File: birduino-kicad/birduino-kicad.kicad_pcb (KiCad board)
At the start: 2 copper layers, 40.1 x 63.2 mm, 1 part, among them U1 ATMEGA328-PU

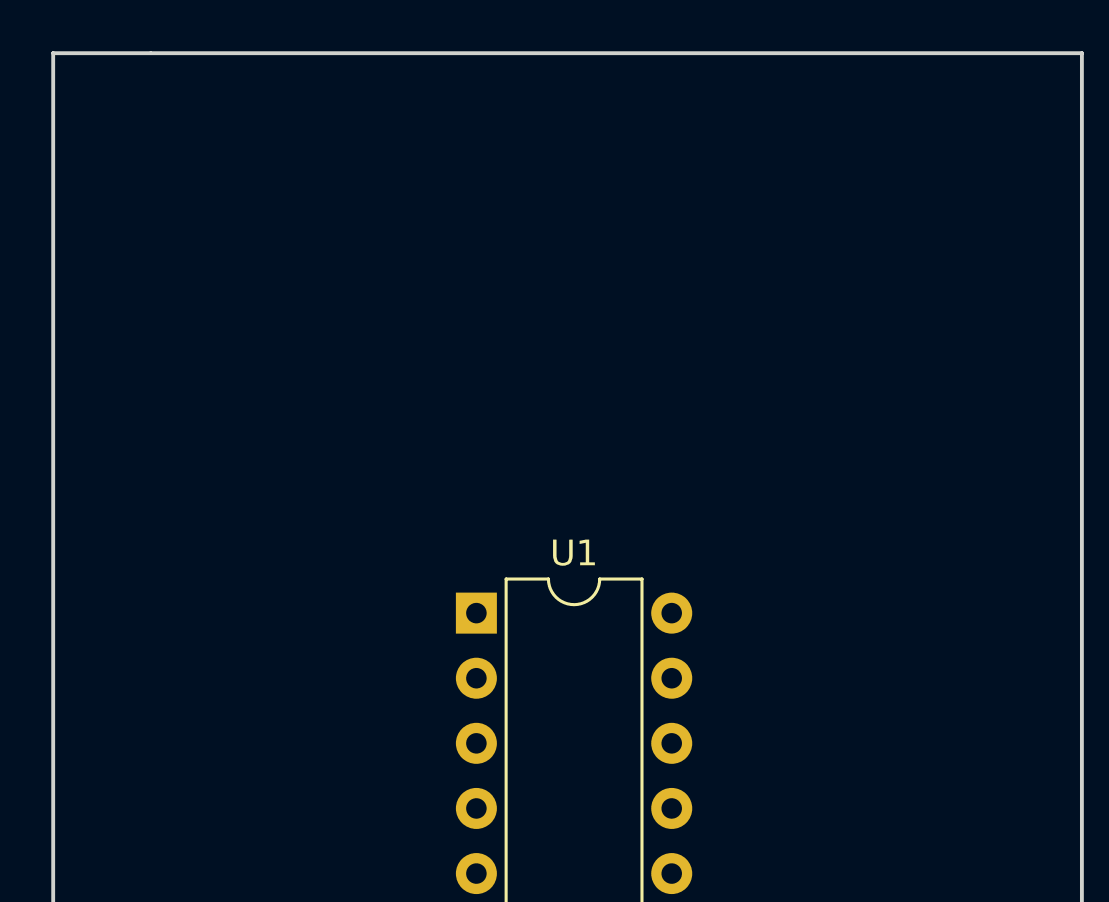
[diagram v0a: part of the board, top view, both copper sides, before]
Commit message: feat: Added more components to the board
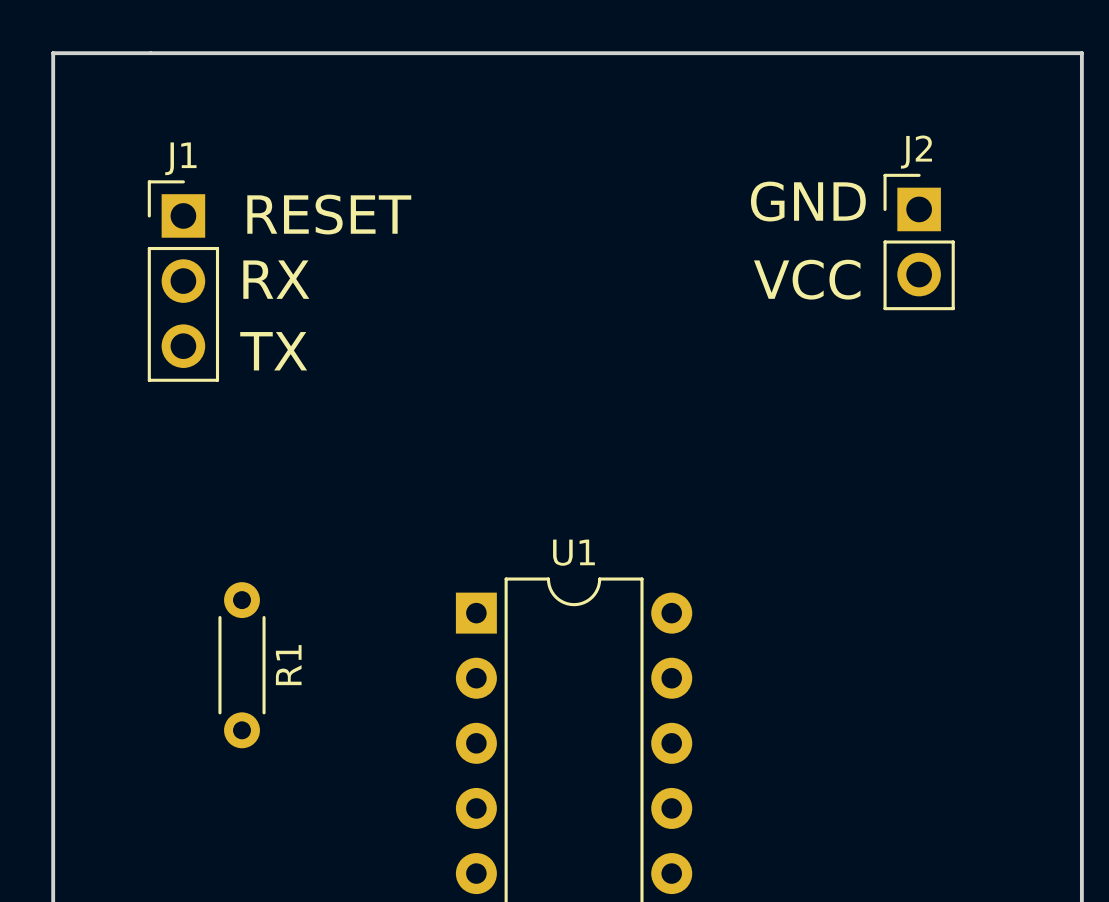
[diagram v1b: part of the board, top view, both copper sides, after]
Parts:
- added J1: Conn_01x03_Male, Pin_Headers:Pin_Header_Straight_1x03_Pitch2.54mm, F.Cu at (144.8, 65.5)
- added J2: Conn_01x02_Male, Pin_Headers:Pin_Header_Straight_1x02_Pitch2.54mm, F.Cu at (173.5, 65.3)
- added R1: 10k, Resistors_THT:R_Axial_DIN0204_L3.6mm_D1.6mm_P5.08mm_Horizontal, F.Cu at (147.1, 80.5)
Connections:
- U1 pad 1: (no net) -> Net-(J1-Pad1)
- U1 pad 2: (no net) -> Net-(J1-Pad2)
- U1 pad 20: (no net) -> Net-(J2-Pad2)
- U1 pad 22: (no net) -> GND
- U1 pad 3: (no net) -> Net-(J1-Pad3)
- U1 pad 7: (no net) -> Net-(J2-Pad2)
- U1 pad 8: (no net) -> GND
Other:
- board text added: "GND"
- board text added: "RESET"
- board text added: "RX"
- board text added: "TX"
- board text added: "VCC"

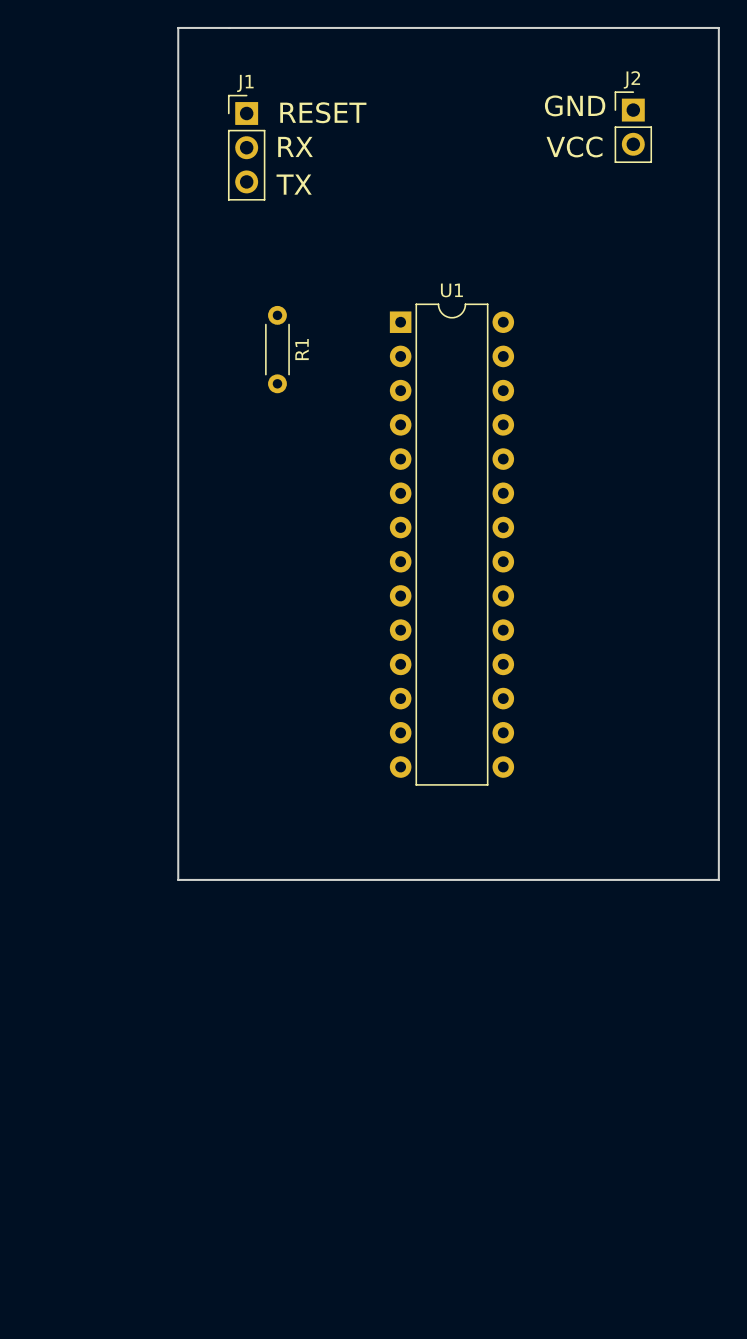
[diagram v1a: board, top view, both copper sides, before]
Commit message: feat: add radio card connections, added the first routing of vias, added backside label.
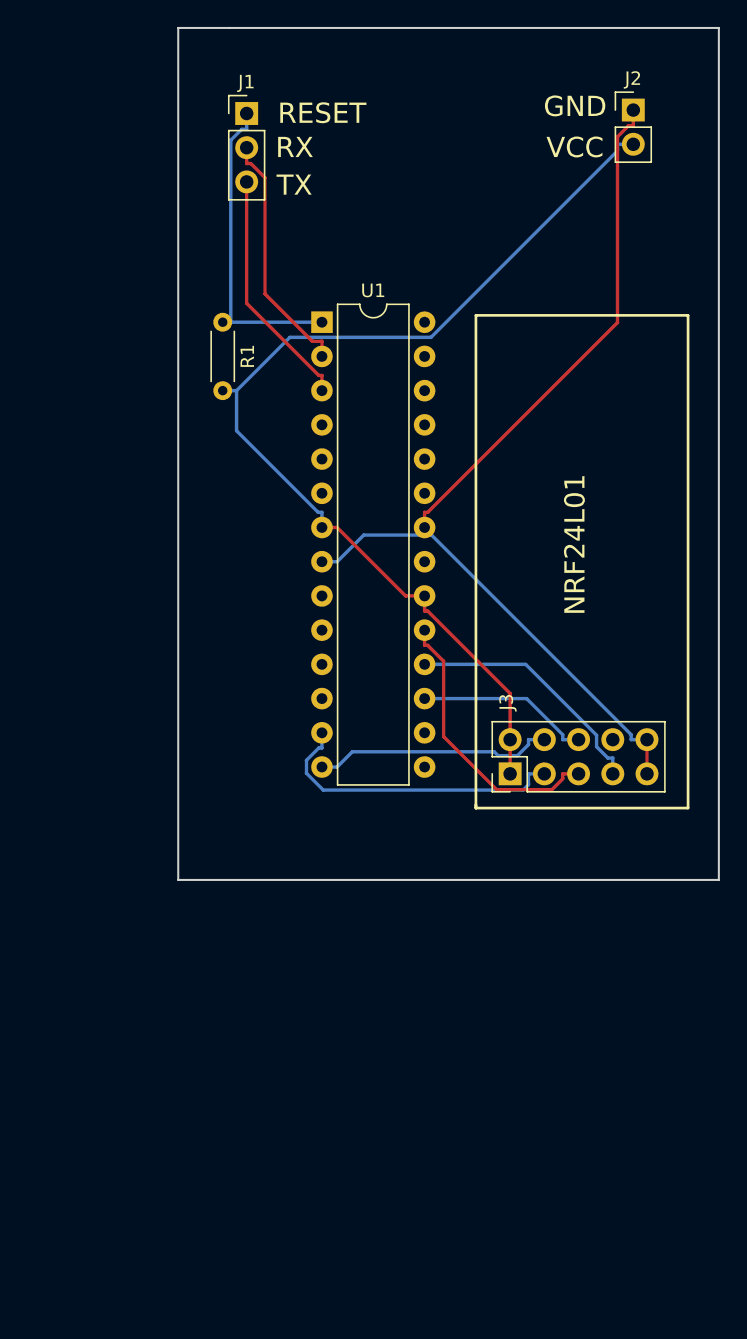
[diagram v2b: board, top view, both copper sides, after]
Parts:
- added J3: Conn_02x05_Odd_Even, Pin_Headers:Pin_Header_Straight_2x05_Pitch2.54mm, F.Cu at (164.3, 114.6)
- moved U1 5.84 mm to (150.4, 81.0)
- moved R1 4.10 mm to (143.0, 81.0)
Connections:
- net Net-(J2-Pad2) renamed VCC
- U1 pad 13: (no net) -> CE
- U1 pad 14: (no net) -> CSN
- U1 pad 17: (no net) -> MO
- U1 pad 18: (no net) -> MI
- U1 pad 19: (no net) -> SCK
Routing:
- net VCC: track 0.00 -> 77.0 mm
- net GND: track 0.00 -> 72.3 mm
- net Net-(J1-Pad1): track 0.00 -> 23.6 mm
- net CE: track 0.00 -> 22.8 mm
- net SCK: track 0.00 -> 21.0 mm
- net MI: track 0.00 -> 18.5 mm
- net Net-(J1-Pad2): track 0.00 -> 18.4 mm
- net Net-(J1-Pad3): track 0.00 -> 17.9 mm
- net CSN: track 0.00 -> 17.8 mm
- net MO: track 0.00 -> 12.9 mm
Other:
- board text added: "NRF24L01"
- board text added: "birduino v. 1.0 Designed in Berlin (02.2019)"

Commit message: feat: add footprint to the buttons, new routing with butons.
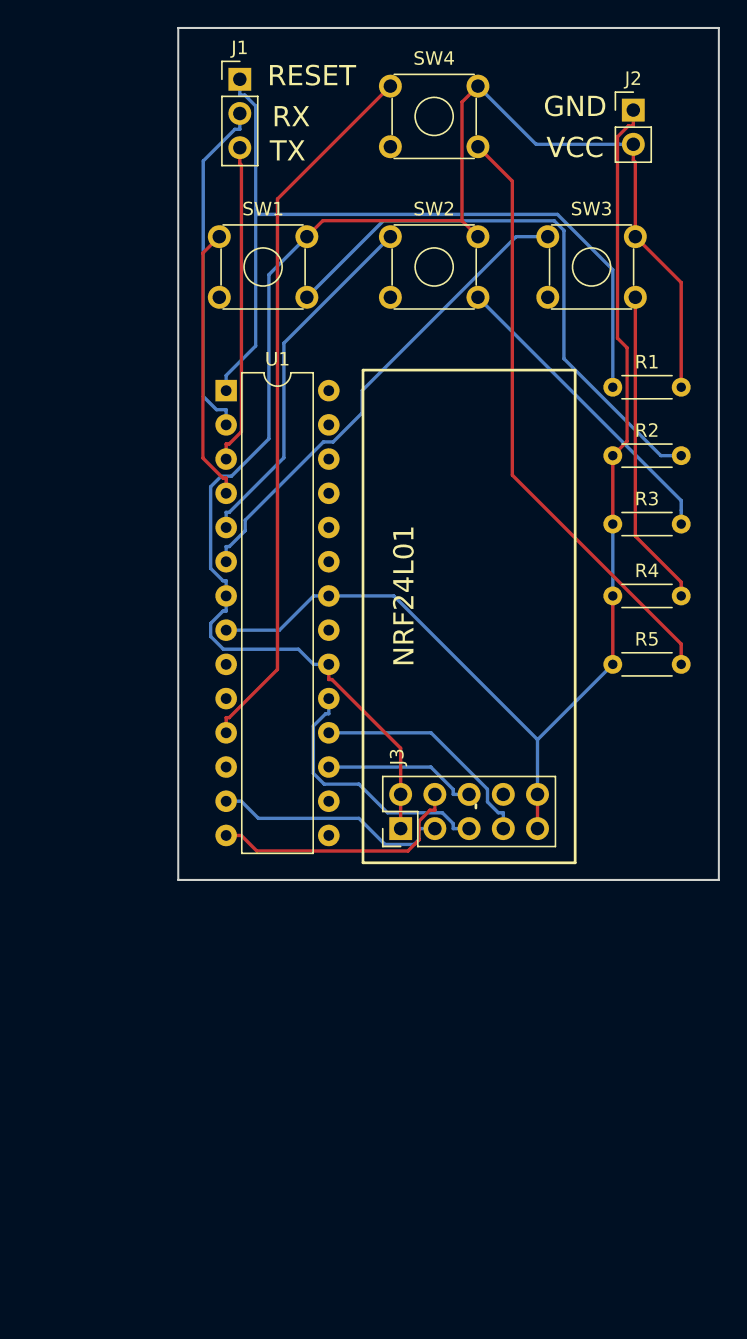
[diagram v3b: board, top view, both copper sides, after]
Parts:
- added R2: 10k, Resistors_THT:R_Axial_DIN0204_L3.6mm_D1.6mm_P5.08mm_Horizontal, F.Cu at (172.0, 90.9)
- added R3: 10k, Resistors_THT:R_Axial_DIN0204_L3.6mm_D1.6mm_P5.08mm_Horizontal, F.Cu at (172.0, 96.0)
- added R4: 10k, Resistors_THT:R_Axial_DIN0204_L3.6mm_D1.6mm_P5.08mm_Horizontal, F.Cu at (172.0, 101.3)
- added R5: 10k, Resistors_THT:R_Axial_DIN0204_L3.6mm_D1.6mm_P5.08mm_Horizontal, F.Cu at (172.0, 106.4)
- added SW1: SW_Push_Dual, Buttons_Switches_THT:SW_TH_Tactile_Omron_B3F-10xx, F.Cu at (142.7, 74.7)
- added SW2: SW_Push_Dual, Buttons_Switches_THT:SW_TH_Tactile_Omron_B3F-10xx, F.Cu at (155.4, 74.7)
- added SW3: SW_Push_Dual, Buttons_Switches_THT:SW_TH_Tactile_Omron_B3F-10xx, F.Cu at (167.1, 74.7)
- added SW4: SW_Push_Dual, Buttons_Switches_THT:SW_TH_Tactile_Omron_B3F-10xx, F.Cu at (155.4, 63.5)
- moved R1 29.4 mm to (172.0, 85.9), turned to 0 degrees
- moved J3 9.09 mm to (156.2, 118.6)
- moved U1 8.74 mm to (143.3, 86.1)
- moved J1 2.59 mm to (144.3, 63.0)
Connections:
- U1 pad 11: (no net) -> BT4
- U1 pad 4: (no net) -> BT1
- U1 pad 5: (no net) -> BT2
- U1 pad 6: (no net) -> BT3
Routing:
- net BT4: track 0.00 -> 53.2 mm
- net Net-(R5-Pad2): track 0.00 -> 44.7 mm
- net Net-(R2-Pad2): track 0.00 -> 42.9 mm
- net VCC: track 77.0 -> 115.5 mm
- net Net-(J1-Pad1): track 23.6 -> 61.7 mm
- net BT3: track 0.00 -> 36.0 mm
- net BT2: track 0.00 -> 26.8 mm
- net Net-(R4-Pad2): track 0.00 -> 23.6 mm
- net Net-(R3-Pad2): track 0.00 -> 23.1 mm
- net BT1: track 0.00 -> 20.4 mm
- net GND: track 72.3 -> 85.7 mm
- net Net-(J1-Pad2): track 18.4 -> 25.6 mm
- net Net-(J1-Pad3): track 17.9 -> 23.8 mm
- net CE: track 22.8 -> 17.8 mm
- net MO: track 12.9 -> 11.5 mm
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
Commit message: feat: add display to board
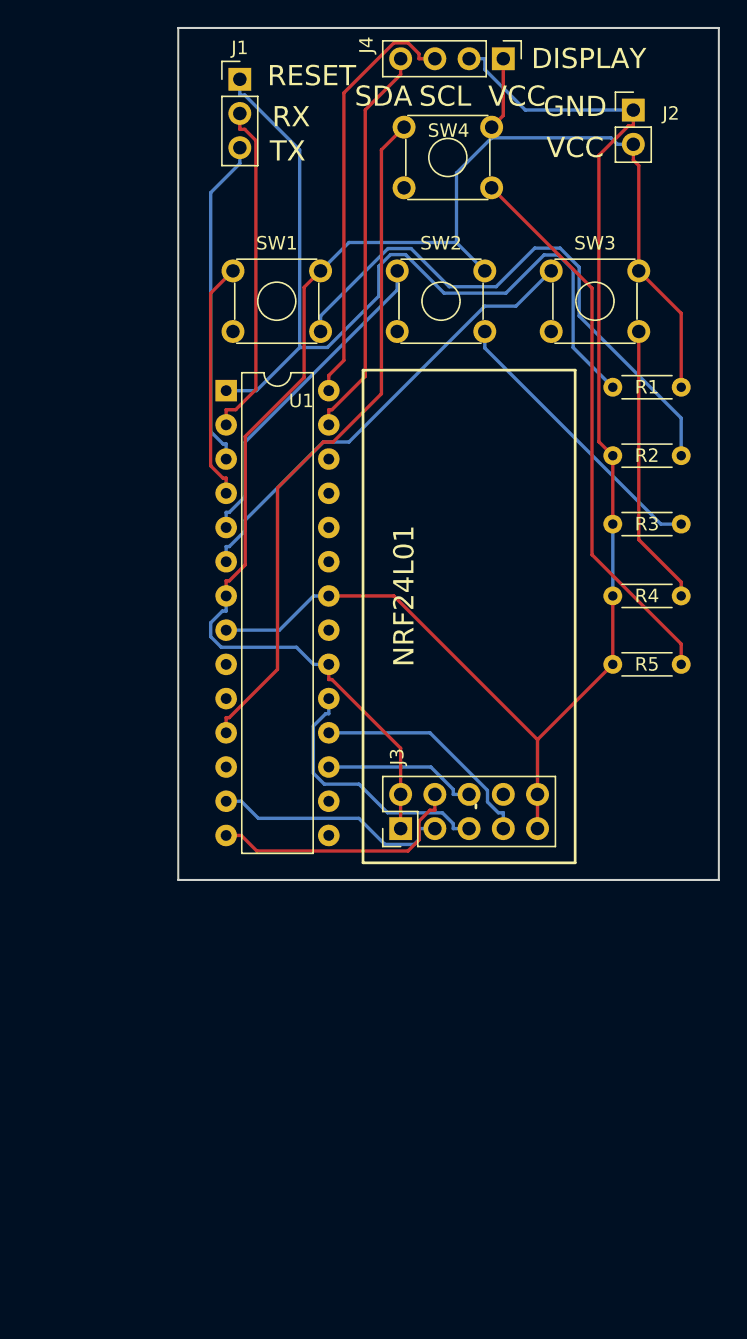
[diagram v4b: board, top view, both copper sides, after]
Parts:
- added J4: Conn_01x04, Pin_Headers:Pin_Header_Straight_1x04_Pitch2.54mm, F.Cu at (163.8, 61.5)
- moved SW4 3.21 mm to (156.5, 66.5)
- moved SW1 2.74 mm to (143.8, 77.2)
- moved SW2 2.59 mm to (156.0, 77.2)
- moved SW3 2.55 mm to (167.4, 77.2)
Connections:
- U1 pad 27: (no net) -> SDA
- U1 pad 28: (no net) -> SCL
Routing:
- net SCL: track 0.00 -> 31.6 mm
- net SDA: track 0.00 -> 29.5 mm
- net GND: track 85.7 -> 100.2 mm
- net Net-(J1-Pad1): track 61.7 -> 66.0 mm
- net Net-(R5-Pad2): track 44.7 -> 41.2 mm
- net Net-(R4-Pad2): track 23.6 -> 20.9 mm
- net BT1: track 20.4 -> 17.8 mm
- net BT2: track 26.8 -> 24.4 mm
- net BT4: track 53.2 -> 51.0 mm
- net Net-(R3-Pad2): track 23.1 -> 21.2 mm
- net BT3: track 36.0 -> 34.2 mm
- net VCC: track 115.5 -> 114.2 mm
- net Net-(J1-Pad3): track 23.8 -> 24.6 mm
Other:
- board text added: "DISPLAY"
- board text added: "SCL"
- board text added: "SDA"

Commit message: feat: migrate to Kicad 5, add LEDs control, add temperature sensor.
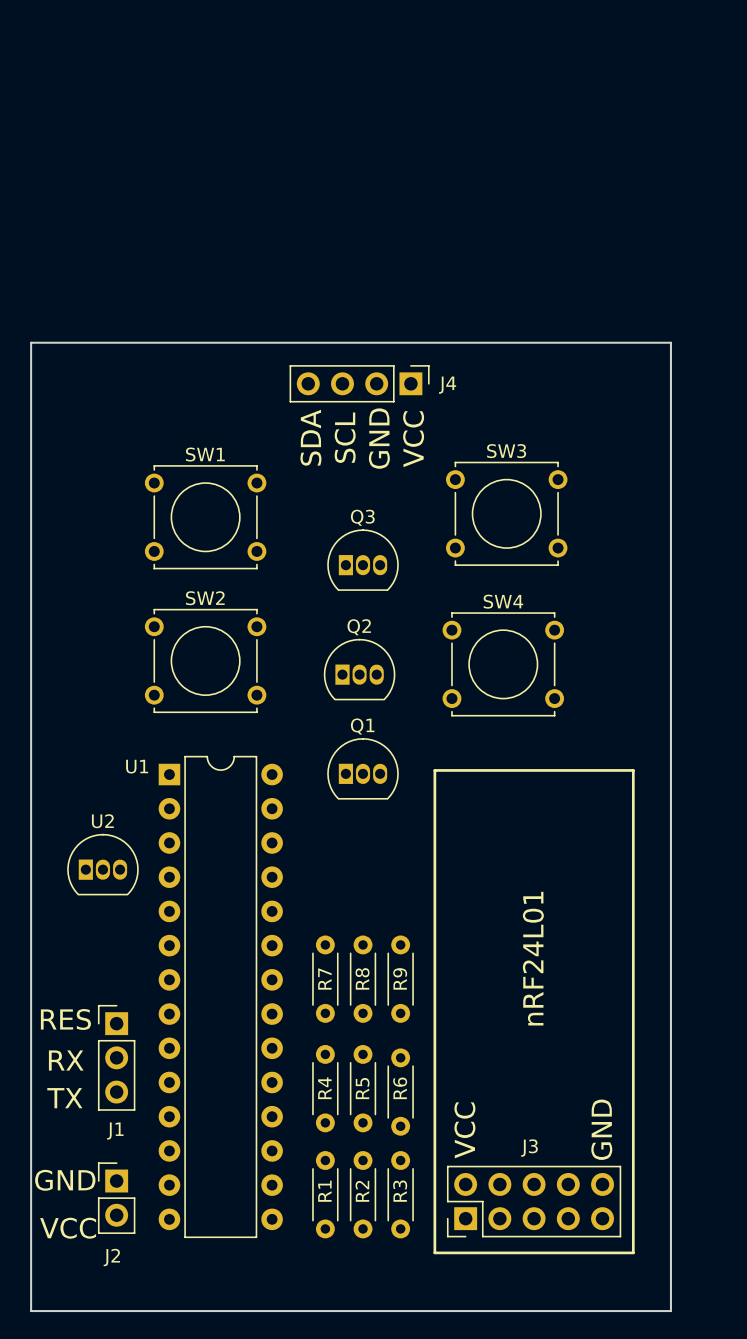
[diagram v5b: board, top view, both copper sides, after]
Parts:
- added Q1: 2N7000, Package_TO_SOT_THT:TO-92_Inline, F.Cu at (152.1, 114.6)
- added Q2: 2N7000, Package_TO_SOT_THT:TO-92_Inline, F.Cu at (151.9, 107.2)
- added Q3: 2N7000, Package_TO_SOT_THT:TO-92_Inline, F.Cu at (152.1, 99.1)
- added R6: 4.7k, Resistor_THT:R_Axial_DIN0204_L3.6mm_D1.6mm_P5.08mm_Horizontal, F.Cu at (156.2, 140.7)
- added R7: 10k, Resistor_THT:R_Axial_DIN0204_L3.6mm_D1.6mm_P5.08mm_Horizontal, F.Cu at (150.6, 132.3)
- added R8: 10k, Resistor_THT:R_Axial_DIN0204_L3.6mm_D1.6mm_P5.08mm_Horizontal, F.Cu at (153.4, 132.3)
- added R9: 10k, Resistor_THT:R_Axial_DIN0204_L3.6mm_D1.6mm_P5.08mm_Horizontal, F.Cu at (156.2, 132.3)
- added U2: DS18B20, Package_TO_SOT_THT:TO-92_Inline, F.Cu at (132.8, 121.7)
- J1: footprint Pin_Headers:Pin_Header_Straight_1x03_Pitch2.54mm -> Connector_PinHeader_2.54mm:PinHeader_1x03_P2.54mm_Vertical
- J2: footprint Pin_Headers:Pin_Header_Straight_1x02_Pitch2.54mm -> Connector_PinHeader_2.54mm:PinHeader_1x02_P2.54mm_Vertical
- J3: footprint Pin_Headers:Pin_Header_Straight_2x05_Pitch2.54mm -> Connector_PinHeader_2.54mm:PinHeader_2x05_P2.54mm_Vertical
- J4: footprint Pin_Headers:Pin_Header_Straight_1x04_Pitch2.54mm -> Connector_PinHeader_2.54mm:PinHeader_1x04_P2.54mm_Vertical
- R1, R2, R3, R4, R5: footprint Resistors_THT:R_Axial_DIN0204_L3.6mm_D1.6mm_P5.08mm_Horizontal -> Resistor_THT:R_Axial_DIN0204_L3.6mm_D1.6mm_P5.08mm_Horizontal
- SW1, SW2, SW3, SW4: footprint Buttons_Switches_THT:SW_TH_Tactile_Omron_B3F-10xx -> Button_Switch_THT:SW_Tactile_Straight_KSA0Axx1LFTR
- U1: footprint Housings_DIP:DIP-28_W7.62mm -> Package_DIP:DIP-28_W7.62mm
- moved J2 88.3 mm to (135.1, 144.8)
- moved J1 70.7 mm to (135.1, 133.1)
- moved R1 66.0 mm to (150.6, 148.3), turned to 90 degrees
- moved R2 60.3 mm to (153.4, 148.3), turned to 90 degrees
- moved R3 54.6 mm to (156.2, 148.3), turned to 90 degrees
- moved R4 44.6 mm to (150.6, 140.5), turned to 90 degrees
- moved R5 38.8 mm to (153.4, 140.5), turned to 90 degrees
- moved SW4 37.5 mm to (160.0, 103.9)
- moved SW2 32.0 mm to (137.9, 103.6)
- moved J3 29.4 mm to (161.0, 147.6)
- moved U1 28.8 mm to (139.0, 114.6)
- moved J4 25.1 mm to (157.0, 85.6)
- moved SW3 17.0 mm to (160.3, 92.7)
- moved SW1 16.8 mm to (137.9, 93.0)
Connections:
- R2 pad 2: Net-(R2-Pad2) -> (no net)
- R3 pad 2: Net-(R3-Pad2) -> (no net)
- R4 pad 2: Net-(R4-Pad2) -> (no net)
- R5 pad 2: Net-(R5-Pad2) -> (no net)
- U1 pad 15: (no net) -> TEMP
- U1 pad 23: (no net) -> LED1
- U1 pad 24: (no net) -> LED2
- U1 pad 25: (no net) -> LED3
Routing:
- net VCC: track 114.2 -> 0.00 mm
- net GND: track 100.2 -> 0.00 mm
- net Net-(J1-Pad1): track 66.0 -> 0.00 mm
- net BT4: track 51.0 -> 0.00 mm
- net Net-(R2-Pad2): track 42.5 -> 0.00 mm
- net Net-(R5-Pad2): track 41.2 -> 0.00 mm
- net BT3: track 34.2 -> 0.00 mm
- net SCL: track 31.6 -> 0.00 mm
- net SDA: track 29.5 -> 0.00 mm
- net Net-(J1-Pad2): track 25.2 -> 0.00 mm
- net Net-(J1-Pad3): track 24.6 -> 0.00 mm
- net BT2: track 24.4 -> 0.00 mm
- net Net-(R3-Pad2): track 21.2 -> 0.00 mm
- net Net-(R4-Pad2): track 20.9 -> 0.00 mm
- net SCK: track 19.6 -> 0.00 mm
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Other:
- board size 40.1 x 63.2 mm -> 47.5 x 71.9 mm
- board text added: "RES"
- board text added: "nRF24L01"
- board text removed: "DISPLAY"
- board text removed: "NRF24L01"
- board text removed: "RESET"
- board text removed: "birduino v. 1.0 Designed in Berlin (02.2019)"
